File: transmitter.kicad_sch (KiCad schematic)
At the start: 0 parts

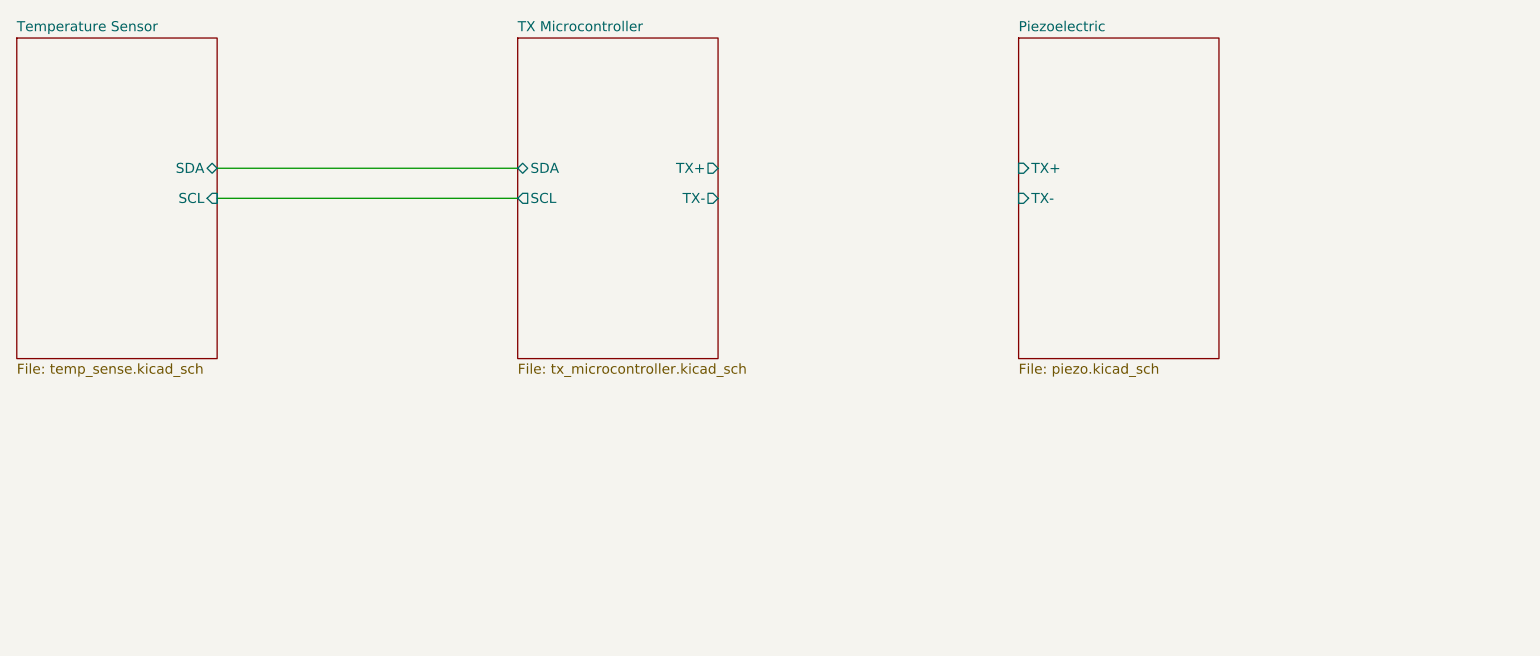
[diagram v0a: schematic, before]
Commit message: Added USB to UART circuitry, cleaned up top sheets, added more supporting circuitry for TX MCU
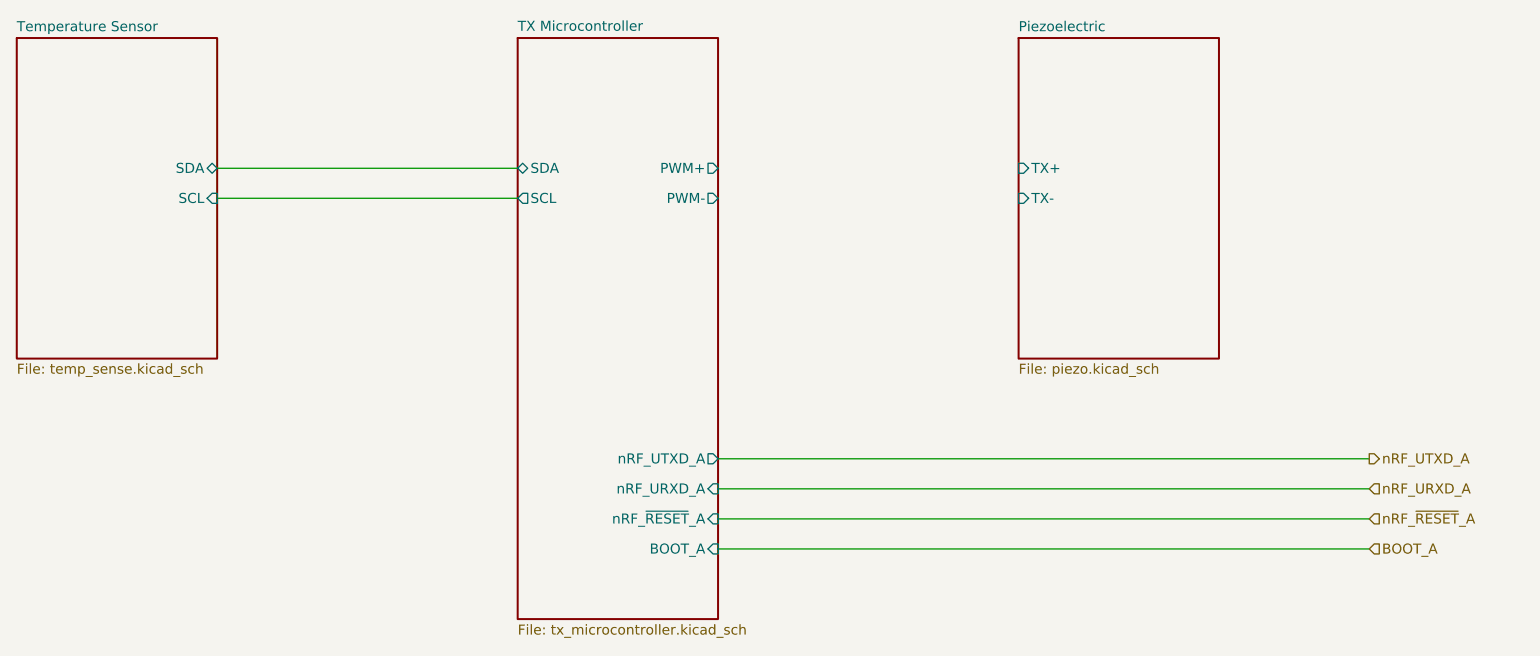
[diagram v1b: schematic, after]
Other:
- sheet TX Microcontroller ports: added BOOT_A, PWM+, PWM-, nRF_URXD_A, nRF_UTXD_A, nRF_~{RESET}_A; removed TX+, TX-
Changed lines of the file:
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@@
+	(wire
+		(pts
+			(xy 161.29 139.7) (xy 243.84 139.7)
+		)
+		(stroke
+			(width 0)
+			(type default)
+		)
+	)
+	(wire
+		(pts
+			(xy 161.29 135.89) (xy 243.84 135.89)
+		)
+		(stroke
+			(width 0)
+			(type default)
+		)
+	)
 	(wire
 		(pts
@@
 	(wire
 		(pts
+			(xy 161.29 132.08) (xy 243.84 132.08)
+		)
+		(stroke
+			(width 0)
+			(type default)
+		)
+	)
+	(wire
+		(pts
 			(xy 97.79 95.25) (xy 135.89 95.25)
 		)
@@
 			(width 0)
 			(type default)
+		)
+	)
+	(wire
+		(pts
+			(xy 161.29 143.51) (xy 243.84 143.51)
+		)
+		(stroke
+			(width 0)
+			(type default)
+		)
+	)
+	(hierarchical_label "nRF_UTXD_A"
+		(shape output)
+		(at 243.84 132.08 0)
+		(effects
+			(font
+				(size 1.27 1.27)
+			)
+			(justify left)
+		)
+	)
+	(hierarchical_label "nRF_~{RESET}_A"
+		(shape input)
+		(at 243.84 139.7 0)
+		(effects
+			(font
+				(size 1.27 1.27)
+			)
+			(justify left)
+		)
+	)
+	(hierarchical_label "BOOT_A"
+		(shape input)
+		(at 243.84 143.51 0)
+		(effects
+			(font
+				(size 1.27 1.27)
+			)
+			(justify left)
+		)
+	)
+	(hierarchical_label "nRF_URXD_A"
+		(shape input)
+		(at 243.84 135.89 0)
+		(effects
+			(font
+				(size 1.27 1.27)
+			)
+			(justify left)
 		)
 	)
@@
 		(fields_autoplaced yes)
 		(stroke
-			(width 0.1524)
+			(width 0.254)
 			(type solid)
 		)
 		(fill
-			(color 0 0 0 0)
+			(color 255 255 194 1)
 		)
 		(property "Sheetname" "Temperature Sensor"
@@
 	(sheet
 		(at 135.89 78.74)
-		(size 25.4 40.64)
+		(size 25.4 73.66)
 		(exclude_from_sim no)
 		(in_bom yes)
@@
 		(fields_autoplaced yes)
 		(stroke
-			(width 0.1524)
+			(width 0.254)
 			(type solid)
 		)
 		(fill
-			(color 0 0 0 0)
+			(color 255 255 194 1)
 		)
 		(property "Sheetname" "TX Microcontroller"
-			(at 135.89 78.0284 0)
+			(at 135.89 77.9776 0)
 			(show_name no)
 			(do_not_autoplace no)
@@
 		)
 		(property "Sheetfile" "tx_microcontroller.kicad_sch"
-			(at 135.89 119.9646 0)
+			(at 135.89 153.0354 0)
 			(show_name no)
 			(do_not_autoplace no)
@@
 				)
 				(justify left top)
-			)
-		)
-		(pin "TX-" output
-			(at 161.29 99.06 0)
-			(effects
-				(font
-					(size 1.27 1.27)
-				)
-				(justify right)
-			)
-		)
-		(pin "TX+" output
-			(at 161.29 95.25 0)
-			(effects
-				(font
-					(size 1.27 1.27)
-				)
-				(justify right)
 			)
 		)
@@
 				)
 				(justify left)
+			)
+		)
+		(pin "BOOT_A" input
+			(at 161.29 143.51 0)
+			(effects
+				(font
+					(size 1.27 1.27)
+				)
+				(justify right)
+			)
+		)
+		(pin "nRF_URXD_A" input
+			(at 161.29 135.89 0)
+			(effects
+				(font
+					(size 1.27 1.27)
+				)
+				(justify right)
+			)
+		)
+		(pin "nRF_~{RESET}_A" input
+			(at 161.29 139.7 0)
+			(effects
+				(font
+					(size 1.27 1.27)
+				)
+				(justify right)
+			)
+		)
+		(pin "nRF_UTXD_A" output
+			(at 161.29 132.08 0)
+			(effects
+				(font
+					(size 1.27 1.27)
+				)
+				(justify right)
+			)
+		)
+		(pin "PWM-" output
+			(at 161.29 99.06 0)
+			(effects
+				(font
+					(size 1.27 1.27)
+				)
+				(justify right)
+			)
+		)
+		(pin "PWM+" output
+			(at 161.29 95.25 0)
+			(effects
+				(font
+					(size 1.27 1.27)
+				)
+				(justify right)
 			)
 		)
@@
 		(fields_autoplaced yes)
 		(stroke
-			(width 0.1524)
+			(width 0.254)
 			(type solid)
 		)
 		(fill
-			(color 0 0 0 0)
+			(color 255 255 194 1)
 		)
 		(property "Sheetname" "Piezoelectric"

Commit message: Finished schematic, added power section for external power (both power supply and battery), added current sensing for TX microcontroller
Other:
- sheet Piezoelectric: file piezo.kicad_sch -> piezo_TX.kicad_sch
- sheet Piezoelectric ports: added PWM+, PWM-; removed TX+, TX-
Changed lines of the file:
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@@
+	(wire
+		(pts
+			(xy 161.29 95.25) (xy 199.39 95.25)
+		)
+		(stroke
+			(width 0)
+			(type default)
+		)
+	)
 	(wire
 		(pts
 			(xy 97.79 95.25) (xy 135.89 95.25)
+		)
+		(stroke
+			(width 0)
+			(type default)
+		)
+	)
+	(wire
+		(pts
+			(xy 161.29 99.06) (xy 199.39 99.06)
 		)
 		(stroke
@@
 			)
 		)
-		(property "Sheetfile" "piezo.kicad_sch"
+		(property "Sheetfile" "piezo_TX.kicad_sch"
 			(at 199.39 119.9646 0)
 			(show_name no)
@@
 			)
 		)
-		(pin "TX-" input
+		(pin "PWM+" input
+			(at 199.39 95.25 180)
+			(effects
+				(font
+					(size 1.27 1.27)
+				)
+				(justify left)
+			)
+		)
+		(pin "PWM-" input
 			(at 199.39 99.06 180)
 			(effects
 				(font
-					(size 1.27 1.27)
-				)
-				(justify left)
-			)
-		)
-		(pin "TX+" input
-			(at 199.39 95.25 180)
-			(effects
-				(font
